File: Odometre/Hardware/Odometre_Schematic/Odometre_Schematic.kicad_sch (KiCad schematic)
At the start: 26 parts, among them IC1 STM32C092FCP6, J1 Conn_01x03_Pin, J2 Conn_01x03_Pin, J3 Conn_Alim, J4 Conn_Laser1, J5 Conn_Laser2, J6 Conn_02x05_Odd_Even, SW1 SW_Push, SW2 SW_SPST, U1 MCP2562-E-SN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

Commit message: réorganisation du schematic
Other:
- note added: "Connecteurs de LASER"
- note added: "Régulateur de tension + Connecteur d'alim"
- note removed: "Connecteurs entrée"
- note removed: "Régulateur de tension"
- moved on the sheet: C1, C2, J3, SW2, U2

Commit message: modif dossier
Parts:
- removed J6: Conn_02x05_Odd_Even, symbol Connector_Generic:Conn_02x05_Odd_Even
- removed SW2: SW_SPST, symbol Switch:SW_SPST
- added J6: Conn_01x06_Pin, symbol Connector:Conn_01x06_Pin
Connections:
- net +3.3V: now also J6.1 (Pin_1)
- net DEBUG_SWCLK: now also J6.2 (Pin_2)
- net DEBUG_SWDIO: now also J6.4 (Pin_4)
- net GND: now also J6.3 (Pin_3)
- net NRST: now also J6.5 (Pin_5)
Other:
- note added: "Connecteurs de LASER (deuxième option de connecteur JRST)"
- note added: "Microcontrôleur STM32C09FCP6 rajouter un GPIO input push pull"
- note added: "Régulateur de tension + Connecteur d'alim (ajouter la led d'alimentation)"
- note removed: "Connecteurs de LASER"
- note removed: "Microcontrôleur STM32C09FCP6"
- note removed: "Régulateur de tension + Connecteur d'alim"

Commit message: modif ioc
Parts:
- added D3: LED_Alim, symbol Device:LED_Small
- added J7: Conn_01x06_Pin, symbol Connector:Conn_01x06_Pin
- added R4: 330, symbol Device:R
- added SW2: Debug_Botton, Button_Switch_THT:SW_PUSH_6mm, symbol Switch:SW_Push
- SW1: value SW_Push -> Reset_Botton
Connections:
- net +12V: now also J3.1 (Pin_1)
- net +3.3V: now also D3.2 (A), J7.5 (Pin_5)
- net GND: now also J7.2 (Pin_2), R4.2, SW2.2
- net TIM2_CH1: now also J7.3 (Pin_3)
- net TIM2_CH2: now also J7.4 (Pin_4)
- net D_Botton: now reaches IC1.11 (GPIO_input)
- net D_Botton: now also SW2.1
- new net: D3.1 (K), R4.1
- no-connect marks 8 -> 7
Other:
- note added: "Boutons"
- note added: "Connecteur LASER_Odomètre type 2"
- note added: "Connecteurs de LASER_Odomètre type 1"
- note added: "LEDs de test"
- note added: "Régulateur de tension + (Connecteur + LED) d'alim"
- note removed: "Connecteurs de LASER (deuxième option de connecteur JRST)"
- note removed: "Régulateur de tension + Connecteur d'alim (ajouter la led d'alimentation)"
- moved on the sheet: C3, C4, C5, C6, D1, D2, H1, H2, H3, H4, J1, J2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

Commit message: modif shematic
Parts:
- added C7: 100nF, symbol Device:C_Small
- added C8, C9: 10µF, Capacitor_SMD:C_0805_2012Metric_Pad1.18x1.45mm_HandSolder, symbol Device:C_Small
- added D4: LED_Trans, symbol Device:LED_Small
- added R5: 330, symbol Device:R
- added U3: LM1117DT-5.0, Package_TO_SOT_SMD:TO-252-3_TabPin2, symbol Regulator_Linear:LM1117DT-5.0
- R2: value 330 -> 100
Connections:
- net +12V: now also C8.1, C9.1, D4.2 (A), U3.2 (VO), U3.3 (VI)
- net +3.3V: now also C7.1
- net GND: now also C7.2, C8.2, C9.2, R5.2, U3.1 (GND)
- net USART1_RX: no longer names the net of IC1.1 (PB7)
- net USART1_TX: no longer names the net of IC1.2 (PC14)
- new net: D4.1 (K), R5.1
- no-connect marks 7 -> 11
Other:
- moved on the sheet: C1, C2, C3, C4, C5, C6, D1, D2, D3, H1, H2, H3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

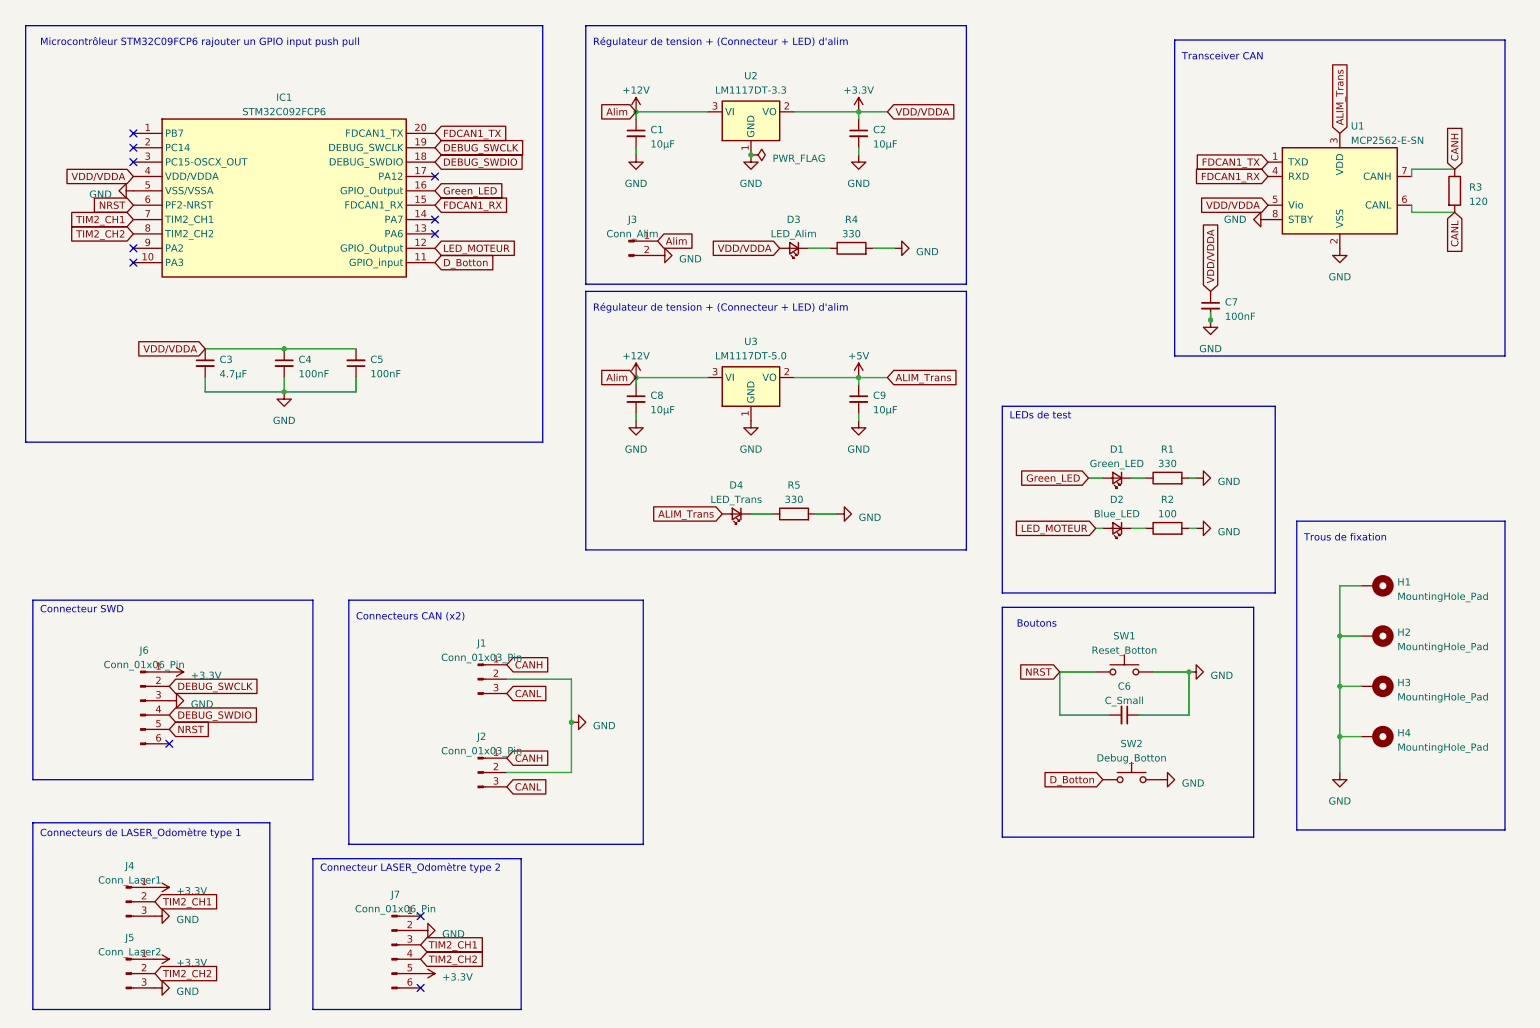
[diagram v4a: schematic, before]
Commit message: ajout d'empreintes
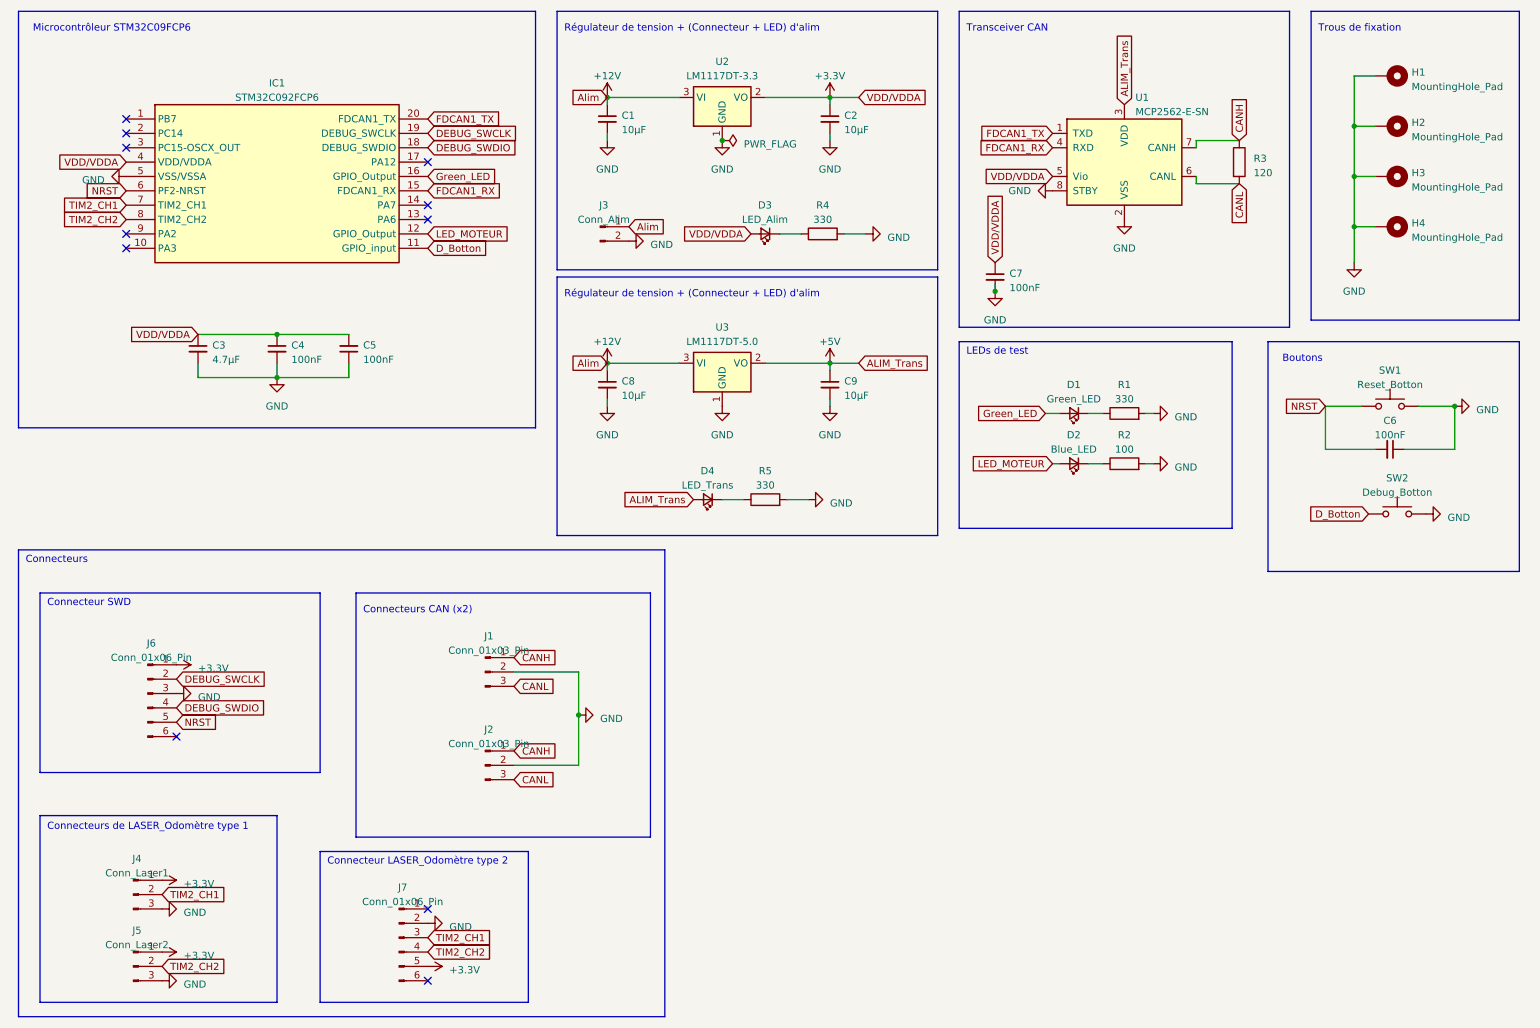
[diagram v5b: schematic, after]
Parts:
- C6: value C_Small -> 100nF
- C7: footprint (none) -> Capacitor_SMD:C_0805_2012Metric_Pad1.18x1.45mm_HandSolder
- D3, D4: footprint (none) -> Diode_SMD:D_0603_1608Metric_Pad1.05x0.95mm_HandSolder
- R4, R5: footprint (none) -> Resistor_SMD:R_0603_1608Metric_Pad0.98x0.95mm_HandSolder
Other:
- note added: "Connecteurs"
- note added: "Microcontrôleur STM32C09FCP6"
- note removed: "Microcontrôleur STM32C09FCP6 rajouter un GPIO input push pull"
- moved on the sheet: C1, C2, C3, C4, C5, C6, C7, C8, C9, D1, D2, D3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

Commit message: Oublie
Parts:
- J1, J2, J6, J7: footprint (none) -> Connector_PinHeader_2.54mm:PinHeader_1x03_P2.54mm_Vertical
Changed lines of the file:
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@@
       (effects (font (size 1.27 1.27)))
     )
-    (property "Footprint" "" (at 99.06 149.86 0)
+    (property "Footprint" "Connector_PinHeader_2.54mm:PinHeader_1x03_P2.54mm_Vertical" (at 99.06 149.86 0)
       (effects (font (size 1.27 1.27)) hide)
     )
@@
       (effects (font (size 1.27 1.27)))
     )
-    (property "Footprint" "" (at 99.06 133.35 0)
+    (property "Footprint" "Connector_PinHeader_2.54mm:PinHeader_1x03_P2.54mm_Vertical" (at 99.06 133.35 0)
       (effects (font (size 1.27 1.27)) hide)
     )
@@
       (effects (font (size 1.27 1.27)))
     )
-    (property "Footprint" "" (at 39.37 137.16 0)
+    (property "Footprint" "Connector_PinHeader_2.54mm:PinHeader_1x03_P2.54mm_Vertical" (at 39.37 137.16 0)
       (effects (font (size 1.27 1.27)) hide)
     )
@@
       (effects (font (size 1.27 1.27)))
     )
-    (property "Footprint" "" (at 83.82 180.34 0)
-      (effects (font (size 1.27 1.27)) hide)
-    )
+    (property "Footprint" "Connector_PinHeader_2.54mm:PinHeader_1x03_P2.54mm_Vertical" (at 83.82 180.34 0)
+      (effects (font (size 1.27 1.27)) hide)
+    )

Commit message: fin schématic
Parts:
- J3: footprint (none) -> Connector_JST:JST_PH_B2B-PH-K_1x02_P2.00mm_Vertical
- J4, J5: footprint (none) -> Connector_PinSocket_2.54mm:PinSocket_1x02_P2.54mm_Vertical

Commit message: all
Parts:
- J7: footprint Connector_PinHeader_2.54mm:PinHeader_1x03_P2.54mm_Vertical -> Connector_JST:JST_PH_B6B-PH-K_1x06_P2.00mm_Vertical
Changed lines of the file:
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@@
 			)
 		)
-		(property "Footprint" "Connector_PinHeader_2.54mm:PinHeader_1x03_P2.54mm_Vertical"
+		(property "Footprint" "Connector_JST:JST_PH_B6B-PH-K_1x06_P2.00mm_Vertical"
 			(at 83.82 180.34 0)
 			(effects
